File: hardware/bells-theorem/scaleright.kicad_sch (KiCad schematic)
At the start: 10 parts, among them U13 MCP6002-xSN

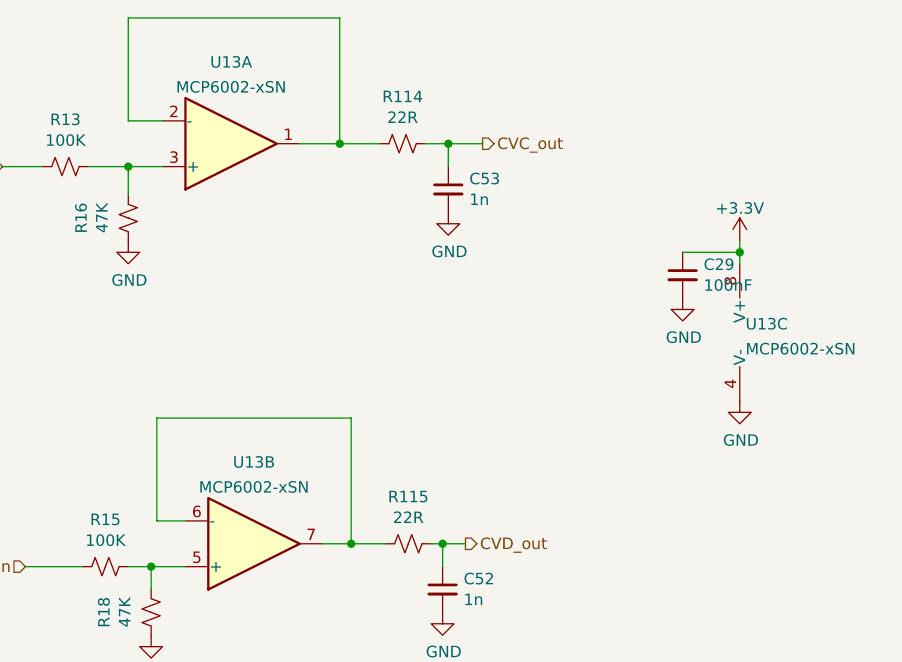
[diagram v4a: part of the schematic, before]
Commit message: current revision actually 0.6 was 1.0 candidate, but needs major revision
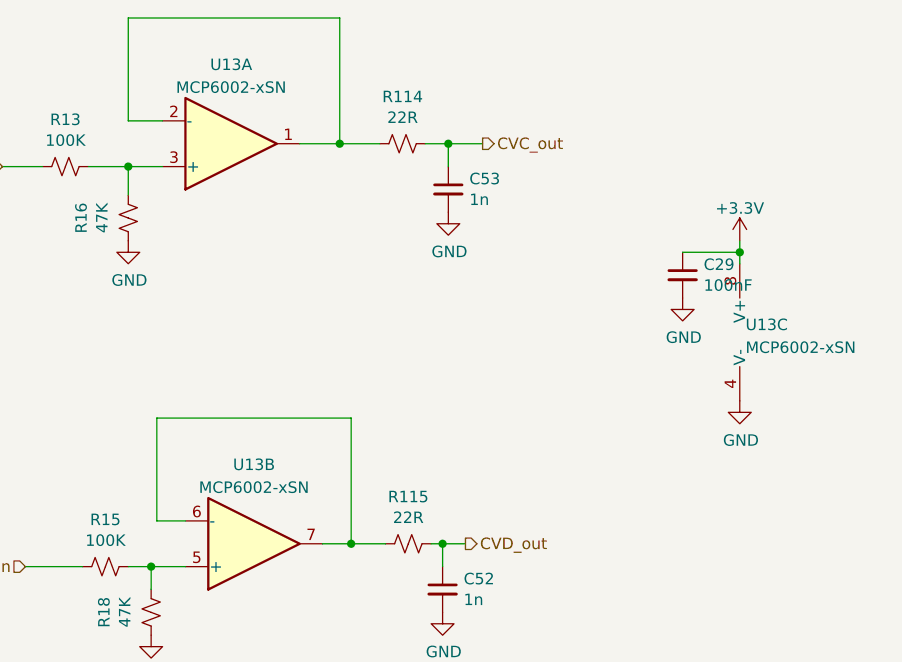
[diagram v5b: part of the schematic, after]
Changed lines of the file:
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@@
   (symbol (lib_id "power:GND") (at 149.86 67.945 0) (unit 1)
     (in_bom yes) (on_board yes)
-    (property "Reference" "#PWR0210" (id 0) (at 149.86 74.295 0)
+    (property "Reference" "#PWR0175" (id 0) (at 149.86 74.295 0)
       (effects (font (size 1.27 1.27)) hide)
     )
@@
   (symbol (lib_id "power:GND") (at 123.19 102.87 0) (unit 1)
     (in_bom yes) (on_board yes)
-    (property "Reference" "#PWR062" (id 0) (at 123.19 109.22 0)
+    (property "Reference" "#PWR0173" (id 0) (at 123.19 109.22 0)
       (effects (font (size 1.27 1.27)) hide)
     )
@@
   (symbol (lib_id "power:GND") (at 123.825 58.42 0) (unit 1)
     (in_bom yes) (on_board yes)
-    (property "Reference" "#PWR065" (id 0) (at 123.825 64.77 0)
+    (property "Reference" "#PWR0174" (id 0) (at 123.825 64.77 0)
       (effects (font (size 1.27 1.27)) hide)
     )
@@
   (symbol (lib_id "power:GND") (at 156.21 79.375 0) (unit 1)
     (in_bom yes) (on_board yes)
-    (property "Reference" "#PWR080" (id 0) (at 156.21 85.725 0)
+    (property "Reference" "#PWR0177" (id 0) (at 156.21 85.725 0)
       (effects (font (size 1.27 1.27)) hide)
     )
@@
   (symbol (lib_id "power:GND") (at 90.805 105.41 0) (unit 1)
     (in_bom yes) (on_board yes)
-    (property "Reference" "#PWR0167" (id 0) (at 90.805 111.76 0)
+    (property "Reference" "#PWR0172" (id 0) (at 90.805 111.76 0)
       (effects (font (size 1.27 1.27)) hide)
     )
@@
   (symbol (lib_id "Amplifier_Operational:MCP6002-xSN") (at 158.75 71.755 0) (unit 3)
     (in_bom yes) (on_board yes) (fields_autoplaced)
-    (property "Reference" "U13" (id 0) (at 156.845 70.8465 0)
-      (effects (font (size 1.27 1.27)) (justify left))
-    )
-    (property "Value" "MCP6002-xSN" (id 1) (at 156.845 73.6216 0)
+    (property "Reference" "U13" (id 0) (at 156.845 70.9203 0)
+      (effects (font (size 1.27 1.27)) (justify left))
+    )
+    (property "Value" "MCP6002-xSN" (id 1) (at 156.845 73.4572 0)
       (effects (font (size 1.27 1.27)) (justify left))
     )
@@
   (symbol (lib_id "Amplifier_Operational:MCP6002-xSN") (at 99.695 50.8 0) (mirror x) (unit 1)
     (in_bom yes) (on_board yes) (fields_autoplaced)
-    (property "Reference" "U13" (id 0) (at 99.695 41.7535 0))
-    (property "Value" "MCP6002-xSN" (id 1) (at 99.695 44.5286 0))
+    (property "Reference" "U13" (id 0) (at 99.695 42.0202 0))
+    (property "Value" "MCP6002-xSN" (id 1) (at 99.695 44.5571 0))
     (property "Footprint" "Package_SO:SOIC-8_3.9x4.9mm_P1.27mm" (id 2) (at 99.695 50.8 0)
       (effects (font (size 1.27 1.27)) hide)
@@
   (symbol (lib_id "Amplifier_Operational:MCP6002-xSN") (at 102.235 95.25 0) (mirror x) (unit 2)
     (in_bom yes) (on_board yes) (fields_autoplaced)
-    (property "Reference" "U13" (id 0) (at 102.235 86.2035 0))
-    (property "Value" "MCP6002-xSN" (id 1) (at 102.235 88.9786 0))
+    (property "Reference" "U13" (id 0) (at 102.235 86.4702 0))
+    (property "Value" "MCP6002-xSN" (id 1) (at 102.235 89.0071 0))
     (property "Footprint" "Package_SO:SOIC-8_3.9x4.9mm_P1.27mm" (id 2) (at 102.235 95.25 0)
       (effects (font (size 1.27 1.27)) hide)
@@
   (symbol (lib_id "power:+3.3V") (at 156.21 61.595 0) (unit 1)
     (in_bom yes) (on_board yes) (fields_autoplaced)
-    (property "Reference" "#PWR074" (id 0) (at 156.21 65.405 0)
+    (property "Reference" "#PWR0176" (id 0) (at 156.21 65.405 0)
       (effects (font (size 1.27 1.27)) hide)
     )
@@
   (symbol (lib_id "power:GND") (at 88.265 61.595 0) (unit 1)
     (in_bom yes) (on_board yes)
-    (property "Reference" "#PWR0166" (id 0) (at 88.265 67.945 0)
-      (effects (font (size 1.27 1.27)) hide)
-    )
+    (property "Reference" "#PWR0171" (id 0) (at 88.265 67.945 0)
+      (effects (font (size 1.27 1.27)) hide)
+    )

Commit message: checking in old outstanding changes prior to debugging with Claude Code
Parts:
- added R146, R147: 300k, Resistor_SMD:R_0805_2012Metric_Pad1.20x1.40mm_HandSolder, symbol Device:R_Small_US
- added R148, R149: 100k, Resistor_SMD:R_0805_2012Metric_Pad1.20x1.40mm_HandSolder, symbol Device:R_Small_US
- R13: value 100K -> 300k
- R15: value 100K -> 300K
- R16: value 47K -> 100k
- R18: value 47K -> 100K
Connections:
- net CVC_in: now also R146.2; no longer R13.2
- net CVD_in: now also R147.2; no longer R15.2
- net at R115.2, U13.7: now also R149.1; no longer U13.6 (-)
- net at R114.2, U13.1: now also R148.1; no longer U13.2 (-)
- new net: R146.1, R148.2, U13.2 (-)
- new net: R147.1, R149.2, U13.6 (-)
- new net +5V: R13.2, R15.2
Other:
- note added: "but remember! it's inverted, so software needs to invert it back"
- note added: "scales -5V to +5V to 0 to 3.3V"
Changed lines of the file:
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@@
   (junction (at 123.19 95.25) (diameter 0) (color 0 0 0 0)
   )
+  (junction (at 87.63 36.83) (diameter 0) (color 0 0 0 0)
+  )
+  (junction (at 91.44 81.28) (diameter 0) (color 0 0 0 0)
+  )
   (junction (at 123.825 50.8) (diameter 0) (color 0 0 0 0)
   )
@@
   (junction (at 113.03 95.25) (diameter 0) (color 0 0 0 0)
   )
+  (wire (pts (xy 73.66 36.83) (xy 80.01 36.83))
+    (stroke (width 0) (type default) (color 0 0 0 0))
+  )
+  (wire (pts (xy 87.63 36.83) (xy 87.63 48.26))
+    (stroke (width 0) (type default) (color 0 0 0 0))
+  )
   (wire (pts (xy 149.86 62.865) (xy 156.21 62.865))
     (stroke (width 0) (type default) (color 0 0 0 0))
   )
-  (wire (pts (xy 91.44 81.28) (xy 113.03 81.28))
-    (stroke (width 0) (type default) (color 0 0 0 0))
-  )
   (wire (pts (xy 90.805 97.79) (xy 90.805 100.33))
     (stroke (width 0) (type default) (color 0 0 0 0))
@@
     (stroke (width 0) (type default) (color 0 0 0 0))
   )
-  (wire (pts (xy 88.265 36.83) (xy 88.265 48.26))
-    (stroke (width 0) (type default) (color 0 0 0 0))
-  )
-  (wire (pts (xy 76.835 97.79) (xy 83.185 97.79))
+  (wire (pts (xy 76.2 97.79) (xy 83.185 97.79))
+    (stroke (width 0) (type default) (color 0 0 0 0))
+  )
+  (wire (pts (xy 104.14 81.28) (xy 113.03 81.28))
     (stroke (width 0) (type default) (color 0 0 0 0))
   )
@@
     (stroke (width 0) (type default) (color 0 0 0 0))
   )
+  (wire (pts (xy 74.93 81.28) (xy 81.28 81.28))
+    (stroke (width 0) (type default) (color 0 0 0 0))
+  )
   (wire (pts (xy 121.285 50.8) (xy 123.825 50.8))
     (stroke (width 0) (type default) (color 0 0 0 0))
@@
     (stroke (width 0) (type default) (color 0 0 0 0))
   )
-  (wire (pts (xy 74.295 53.34) (xy 78.74 53.34))
+  (wire (pts (xy 87.63 36.83) (xy 97.79 36.83))
+    (stroke (width 0) (type default) (color 0 0 0 0))
+  )
+  (wire (pts (xy 91.44 81.28) (xy 99.06 81.28))
+    (stroke (width 0) (type default) (color 0 0 0 0))
+  )
+  (wire (pts (xy 86.36 81.28) (xy 91.44 81.28))
+    (stroke (width 0) (type default) (color 0 0 0 0))
+  )
+  (wire (pts (xy 73.66 53.34) (xy 78.74 53.34))
     (stroke (width 0) (type default) (color 0 0 0 0))
   )
@@
     (stroke (width 0) (type default) (color 0 0 0 0))
   )
-  (wire (pts (xy 88.265 36.83) (xy 111.76 36.83))
+  (wire (pts (xy 85.09 36.83) (xy 87.63 36.83))
     (stroke (width 0) (type default) (color 0 0 0 0))
   )
@@
     (stroke (width 0) (type default) (color 0 0 0 0))
   )
+  (wire (pts (xy 102.87 36.83) (xy 111.76 36.83))
+    (stroke (width 0) (type default) (color 0 0 0 0))
+  )
   (wire (pts (xy 113.03 95.25) (xy 116.84 95.25))
     (stroke (width 0) (type default) (color 0 0 0 0))
   )
-  (wire (pts (xy 88.265 48.26) (xy 92.075 48.26))
+  (wire (pts (xy 87.63 48.26) (xy 92.075 48.26))
     (stroke (width 0) (type default) (color 0 0 0 0))
   )
@@
   (wire (pts (xy 88.265 53.34) (xy 88.265 56.515))
     (stroke (width 0) (type default) (color 0 0 0 0))
+  )
+  (text "but remember! it's inverted, so software needs to invert it back"
+    (at 76.2 25.4 0)
+    (effects (font (size 1.27 1.27)) (justify left bottom))
+  )
+  (text "scales -5V to +5V to 0 to 3.3V" (at 90.17 20.32 0)
+    (effects (font (size 1.27 1.27)) (justify left bottom))
+  )
+  (hierarchical_label "CVC_in" (shape input) (at 73.66 36.83 180)
+    (effects (font (size 1.27 1.27)) (justify right))
   )
   (hierarchical_label "CVC_out" (shape output) (at 127.635 50.8 0)
     (effects (font (size 1.27 1.27)) (justify left))
   )
-  (hierarchical_label "CVD_in" (shape input) (at 76.835 97.79 180)
+  (hierarchical_label "CVD_in" (shape input) (at 74.93 81.28 180)
     (effects (font (size 1.27 1.27)) (justify right))
   )
   (hierarchical_label "CVD_out" (shape output) (at 125.73 95.25 0)
     (effects (font (size 1.27 1.27)) (justify left))
-  )
-  (hierarchical_label "CVC_in" (shape input) (at 74.295 53.34 180)
-    (effects (font (size 1.27 1.27)) (justify right))
   )
   (symbol (lib_id "Device:R_Small_US") (at 119.38 95.25 270) (unit 1)
@@
     (pin "1")
   )
+  (symbol (lib_id "power:+5V") (at 76.2 97.79 0) (unit 1)
+    (in_bom yes) (on_board yes) (fields_autoplaced)
+    (property "Reference" "#PWR0190" (id 0) (at 76.2 101.6 0)
+      (effects (font (size 1.27 1.27)) hide)
+    )
+    (property "Value" "+5V" (id 1) (at 76.2 94.2142 0))
+    (property "Footprint" "" (id 2) (at 76.2 97.79 0)
+      (effects (font (size 1.27 1.27)) hide)
+    )
+    (property "Datasheet" "" (id 3) (at 76.2 97.79 0)
+      (effects (font (size 1.27 1.27)) hide)
+    )
+    (pin "1")
+  )
   (symbol (lib_id "Device:R_Small_US") (at 90.805 102.87 0) (unit 1)
     (in_bom yes) (on_board yes)
     (property "Reference" "R18" (id 0) (at 85.598 102.87 90))
-    (property "Value" "47K" (id 1) (at 87.9094 102.87 90))
+    (property "Value" "100K" (id 1) (at 87.9094 102.87 90))
     (property "Footprint" "Resistor_SMD:R_0805_2012Metric_Pad1.20x1.40mm_HandSolder" (id 2) (at 90.805 102.87 0)
       (effects (font (size 1.27 1.27)) hide)
@@
     (in_bom yes) (on_board yes)
     (property "Reference" "R16" (id 0) (at 83.058 59.055 90))
-    (property "Value" "47K" (id 1) (at 85.3694 59.055 90))
+    (property "Value" "100k" (id 1) (at 85.3694 59.055 90))
     (property "Footprint" "Resistor_SMD:R_0805_2012Metric_Pad1.20x1.40mm_HandSolder" (id 2) (at 88.265 59.055 0)
       (effects (font (size 1.27 1.27)) hide)
     )
     (property "Datasheet" "~" (id 3) (at 88.265 59.055 0)
+      (effects (font (size 1.27 1.27)) hide)
+    )
+    (pin "1")
+    (pin "2")
+  )
+  (symbol (lib_id "Device:R_Small_US") (at 100.33 36.83 270) (unit 1)
+    (in_bom yes) (on_board yes)
+    (property "Reference" "R148" (id 0) (at 100.33 31.623 90))
+    (property "Value" "100k" (id 1) (at 100.33 33.9344 90))
+    (property "Footprint" "Resistor_SMD:R_0805_2012Metric_Pad1.20x1.40mm_HandSolder" (id 2) (at 100.33 36.83 0)
+      (effects (font (size 1.27 1.27)) hide)
+    )
+    (property "Datasheet" "~" (id 3) (at 100.33 36.83 0)
       (effects (font (size 1.27 1.27)) hide)
     )
@@
     (in_bom yes) (on_board yes)
     (property "Reference" "R15" (id 0) (at 85.725 92.583 90))
-    (property "Value" "100K" (id 1) (at 85.725 94.8944 90))
+    (property "Value" "300K" (id 1) (at 85.725 94.8944 90))
     (property "Footprint" "Resistor_SMD:R_0805_2012Metric_Pad1.20x1.40mm_HandSolder" (id 2) (at 85.725 97.79 0)
       (effects (font (size 1.27 1.27)) hide)
     )
     (property "Datasheet" "~" (id 3) (at 85.725 97.79 0)
+      (effects (font (size 1.27 1.27)) hide)
+    )
+    (pin "1")
+    (pin "2")
+  )
+  (symbol (lib_id "Device:R_Small_US") (at 82.55 36.83 270) (unit 1)
+    (in_bom yes) (on_board yes)
+    (property "Reference" "R146" (id 0) (at 82.55 31.623 90))
+    (property "Value" "300k" (id 1) (at 82.55 33.9344 90))
+    (property "Footprint" "Resistor_SMD:R_0805_2012Metric_Pad1.20x1.40mm_HandSolder" (id 2) (at 82.55 36.83 0)
+      (effects (font (size 1.27 1.27)) hide)
+    )
+    (property "Datasheet" "~" (id 3) (at 82.55 36.83 0)
       (effects (font (size 1.27 1.27)) hide)
     )
@@
     (pin "1")
   )
+  (symbol (lib_id "Device:R_Small_US") (at 101.6 81.28 270) (unit 1)
+    (in_bom yes) (on_board yes)
+    (property "Reference" "R149" (id 0) (at 101.6 76.073 90))
+    (property "Value" "100k" (id 1) (at 101.6 78.3844 90))
+    (property "Footprint" "Resistor_SMD:R_0805_2012Metric_Pad1.20x1.40mm_HandSolder" (id 2) (at 101.6 81.28 0)
+      (effects (font (size 1.27 1.27)) hide)
+    )
+    (property "Datasheet" "~" (id 3) (at 101.6 81.28 0)
+      (effects (font (size 1.27 1.27)) hide)
+    )
+    (pin "1")
+    (pin "2")
+  )
   (symbol (lib_id "Device:R_Small_US") (at 81.28 53.34 270) (unit 1)
     (in_bom yes) (on_board yes)
     (property "Reference" "R13" (id 0) (at 81.28 48.133 90))
-    (property "Value" "100K" (id 1) (at 81.28 50.4444 90))
+    (property "Value" "300k" (id 1) (at 81.28 50.4444 90))
     (property "Footprint" "Resistor_SMD:R_0805_2012Metric_Pad1.20x1.40mm_HandSolder" (id 2) (at 81.28 53.34 0)
       (effects (font (size 1.27 1.27)) hide)
@@
     (pin "1")
     (pin "2")
+  )
+  (symbol (lib_id "power:+5V") (at 73.66 53.34 0) (unit 1)
+    (in_bom yes) (on_board yes) (fields_autoplaced)
+    (property "Reference" "#PWR0189" (id 0) (at 73.66 57.15 0)
+      (effects (font (size 1.27 1.27)) hide)
+    )
+    (property "Value" "+5V" (id 1) (at 73.66 49.7642 0))
+    (property "Footprint" "" (id 2) (at 73.66 53.34 0)
+      (effects (font (size 1.27 1.27)) hide)
+    )
+    (property "Datasheet" "" (id 3) (at 73.66 53.34 0)
+      (effects (font (size 1.27 1.27)) hide)
+    )
+    (pin "1")
   )
   (symbol (lib_id "power:GND") (at 88.265 61.595 0) (unit 1)
@@
     (pin "1")
   )
+  (symbol (lib_id "Device:R_Small_US") (at 83.82 81.28 270) (unit 1)
+    (in_bom yes) (on_board yes)
+    (property "Reference" "R147" (id 0) (at 83.82 76.073 90))
+    (property "Value" "300k" (id 1) (at 83.82 78.3844 90))
+    (property "Footprint" "Resistor_SMD:R_0805_2012Metric_Pad1.20x1.40mm_HandSolder" (id 2) (at 83.82 81.28 0)
+      (effects (font (size 1.27 1.27)) hide)
+    )
+    (property "Datasheet" "~" (id 3) (at 83.82 81.28 0)
+      (effects (font (size 1.27 1.27)) hide)
+    )
+    (pin "1")
+    (pin "2")
+  )
 )
